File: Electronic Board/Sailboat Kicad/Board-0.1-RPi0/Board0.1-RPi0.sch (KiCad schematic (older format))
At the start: 22 parts, among them J1 Conn_02x20_Odd_Even, J10 Conn_01x03, J11 Conn_01x03, J12 Conn_01x03, J2 Conn_02x12_Odd_Even, J3 Conn_01x01, J4 Conn_02x12_Odd_Even, J5 Conn_01x01, J6 Conn_02x12_Odd_Even, J7 Conn_01x02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

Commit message: Removed the arduino. Why keep it?? Doesn't make sense :/
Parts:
- removed J2, J4, J6: Conn_02x12_Odd_Even, Pin_Headers:Pin_Header_Straight_2x12_Pitch2.54mm, symbol Conn_02x12_Odd_Even
- removed J3, J5: Conn_01x01, Pin_Headers:Pin_Header_Straight_1x01_Pitch2.54mm, symbol Conn_01x01
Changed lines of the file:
@@
 $EndComp
-$Comp
-L Conn_02x12_Odd_Even J2
-U 1 1 5B9A869B
-P 1200 6950
-F 0 "J2" H 1250 7550 50  0000 C CNN
-F 1 "Conn_02x12_Odd_Even" H 1250 6250 50  0000 C CNN
-F 2 "Pin_Headers:Pin_Header_Straight_2x12_Pitch2.54mm" H 1200 6950 50  0001 C CNN
-F 3 "" H 1200 6950 50  0001 C CNN
-	1    1200 6950
-	1    0    0    1
-$EndComp
-$Comp
-L Conn_02x12_Odd_Even J4
-U 1 1 5B9A86F0
-P 2500 5450
-F 0 "J4" H 2550 6050 50  0000 C CNN
-F 1 "Conn_02x12_Odd_Even" H 2550 4750 50  0000 C CNN
-F 2 "Pin_Headers:Pin_Header_Straight_2x12_Pitch2.54mm" H 2500 5450 50  0001 C CNN
-F 3 "" H 2500 5450 50  0001 C CNN
-	1    2500 5450
-	0    1    -1   0
-$EndComp
-$Comp
-L Conn_02x12_Odd_Even J6
-U 1 1 5B9A8755
-P 3700 6950
-F 0 "J6" H 3750 7550 50  0000 C CNN
-F 1 "Conn_02x12_Odd_Even" H 3750 6250 50  0000 C CNN
-F 2 "Pin_Headers:Pin_Header_Straight_2x12_Pitch2.54mm" H 3700 6950 50  0001 C CNN
-F 3 "" H 3700 6950 50  0001 C CNN
-	1    3700 6950
-	1    0    0    1
-$EndComp
-$Comp
-L Conn_01x01 J3
-U 1 1 5B9A8817
-P 1200 5600
-F 0 "J3" H 1200 5700 50  0000 C CNN
-F 1 "Conn_01x01" H 1200 5500 50  0000 C CNN
-F 2 "Pin_Headers:Pin_Header_Straight_1x01_Pitch2.54mm" H 1200 5600 50  0001 C CNN
-F 3 "" H 1200 5600 50  0001 C CNN
-	1    1200 5600
-	1    0    0    -1
-$EndComp
-$Comp
-L Conn_01x01 J5
-U 1 1 5B9A8879
-P 3600 5600
-F 0 "J5" H 3600 5700 50  0000 C CNN
-F 1 "Conn_01x01" H 3600 5500 50  0000 C CNN
-F 2 "Pin_Headers:Pin_Header_Straight_1x01_Pitch2.54mm" H 3600 5600 50  0001 C CNN
-F 3 "" H 3600 5600 50  0001 C CNN
-	1    3600 5600
-	-1   0    0    1
-$EndComp
-$Comp
-L GND #PWR01
-U 1 1 5B9A8D5B
-P 4100 7450
-F 0 "#PWR01" H 4100 7200 50  0001 C CNN
-F 1 "GND" H 4100 7300 50  0000 C CNN
-F 2 "" H 4100 7450 50  0001 C CNN
-F 3 "" H 4100 7450 50  0001 C CNN
-	1    4100 7450
-	1    0    0    -1
-$EndComp
-Wire Wire Line
-	4100 7450 4000 7450
-Wire Wire Line
-	3400 7450 3500 7450
 $Comp
 L +5V #PWR02
@@
 Wire Wire Line
 	2900 800  2800 800
-$Comp
-L +5V #PWR05
-U 1 1 5B9A8D99
-P 3400 7450
-F 0 "#PWR05" H 3400 7300 50  0001 C CNN
-F 1 "+5V" H 3400 7590 50  0000 C CNN
-F 2 "" H 3400 7450 50  0001 C CNN
-F 3 "" H 3400 7450 50  0001 C CNN
-	1    3400 7450
-	-1   0    0    1
-$EndComp
 Text GLabel 5150 800  0    60   Input ~ 0
 BAT+

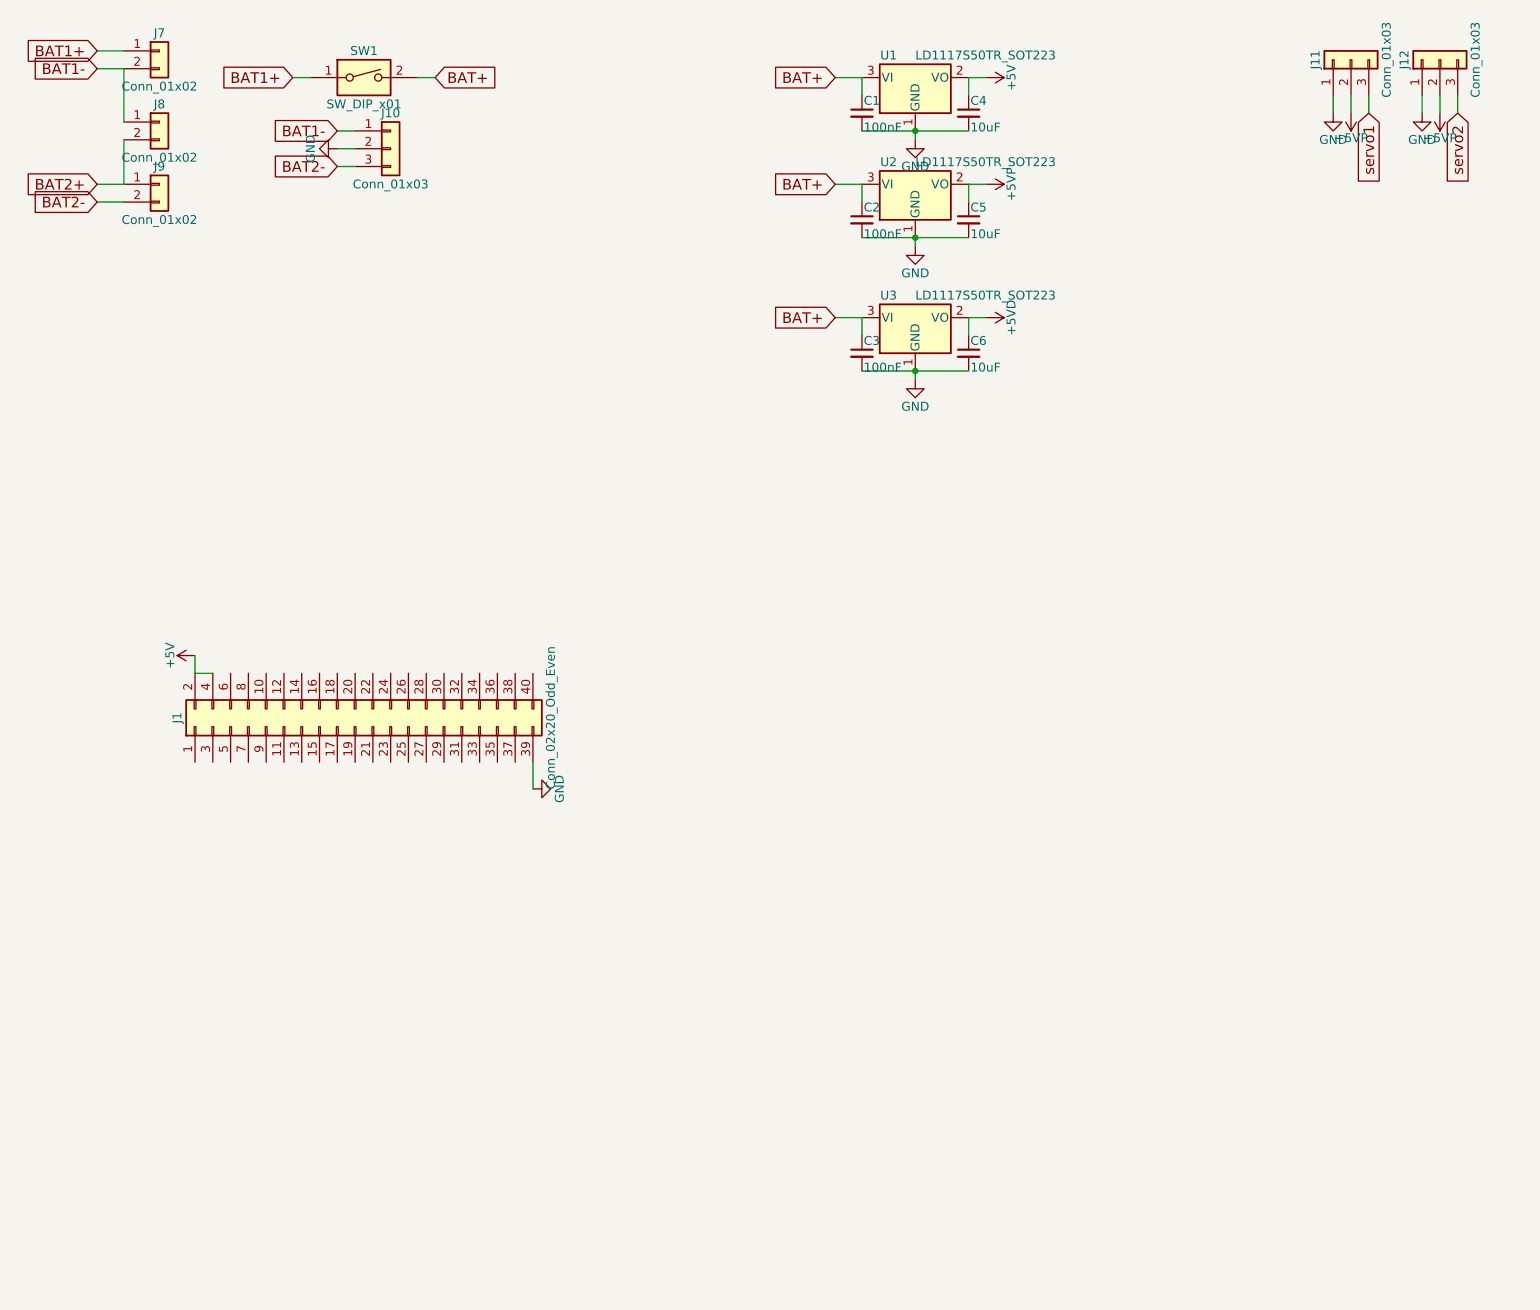
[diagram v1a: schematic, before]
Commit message: Components installed for a working rpi0 shield for sailboat
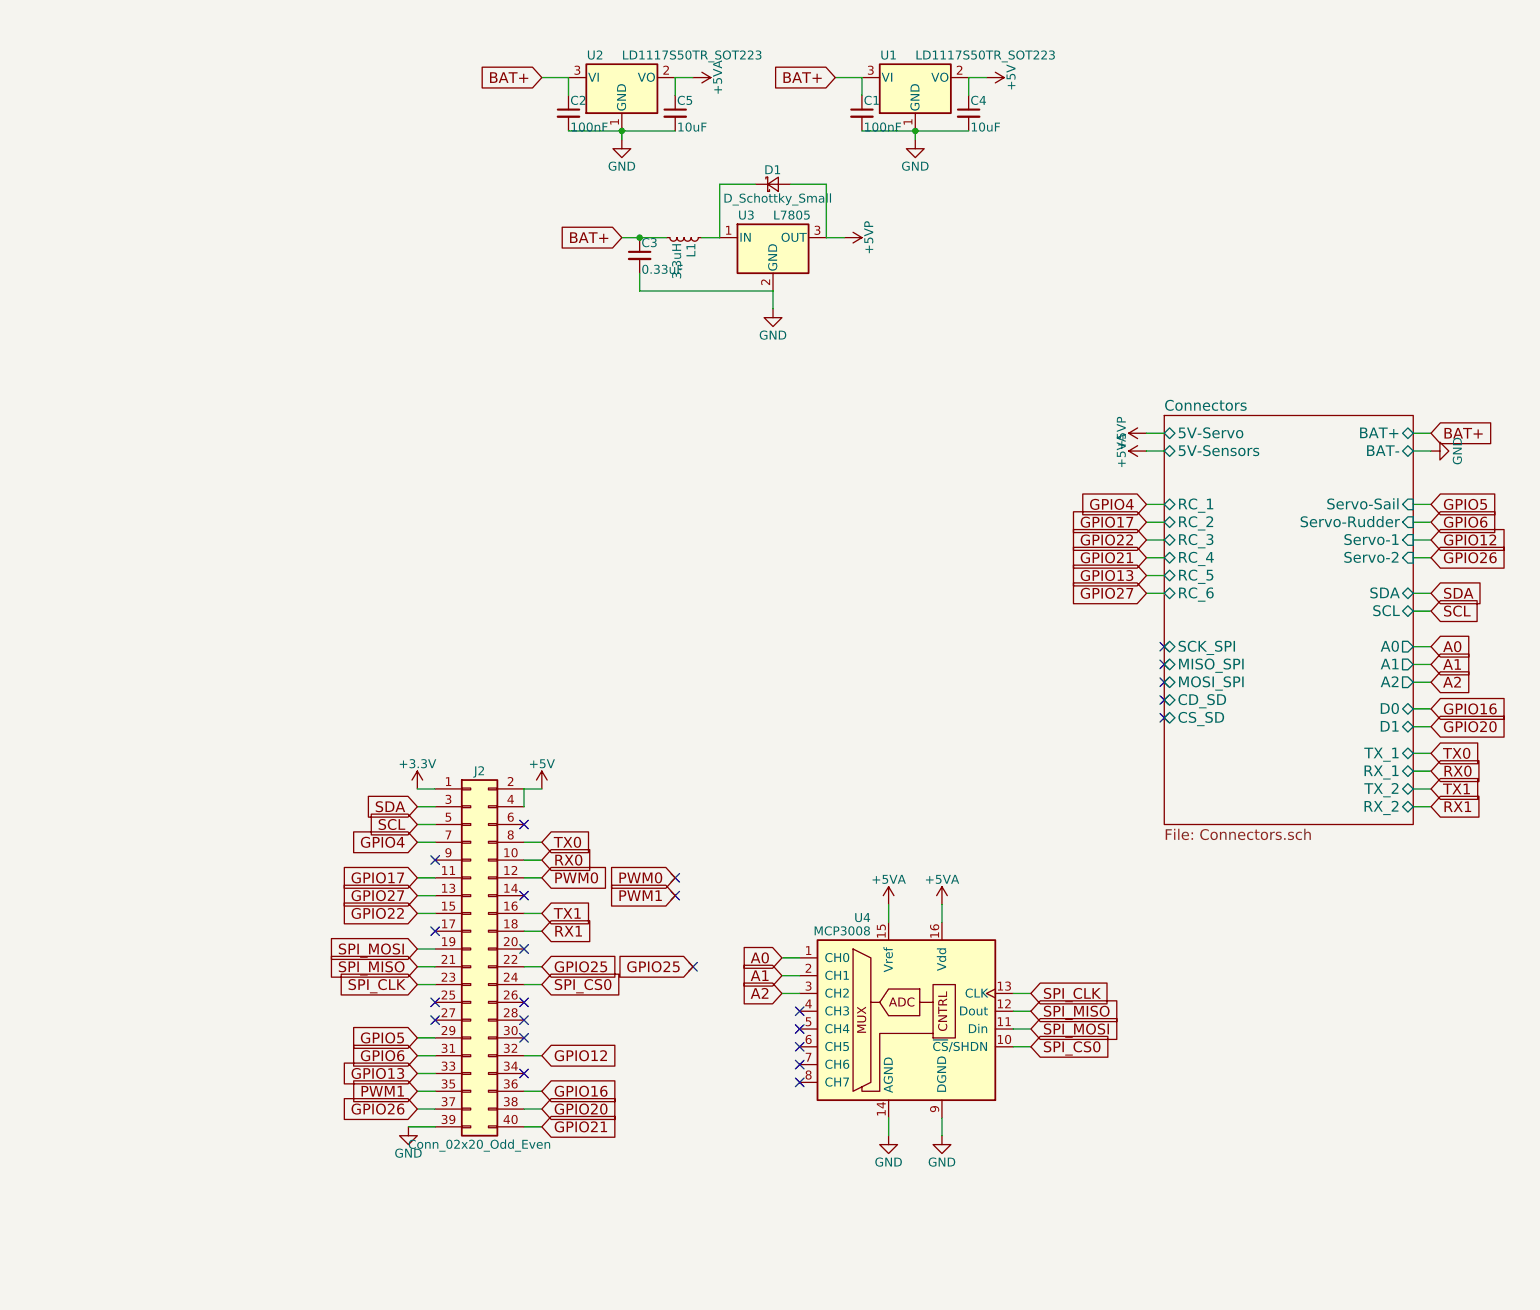
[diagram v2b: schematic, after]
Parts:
- removed C6: 10uF, Capacitors_SMD:C_0603, symbol C_Small
- removed J1: Conn_02x20_Odd_Even, Pin_Headers:Pin_Header_Straight_2x20_Pitch2.54mm, symbol Conn_02x20_Odd_Even
- removed J10: Conn_01x03, Pin_Headers:Pin_Header_Straight_1x03_Pitch2.54mm, symbol Conn_01x03
- removed J11, J12: Conn_01x03, Pin_Headers:Pin_Header_Angled_1x03_Pitch2.54mm, symbol Conn_01x03
- removed J7, J8, J9: Conn_01x02, Pin_Headers:Pin_Header_Straight_1x02_Pitch2.54mm, symbol Conn_01x02
- removed SW1: SW_DIP_x01, Buttons_Switches_THT:SW_DIP_x1_W7.62mm_Slide, symbol SW_DIP_x01
- removed U3: LD1117S50TR_SOT223, TO_SOT_Packages_SMD:SOT-223-3_TabPin2, symbol LD1117S50TR_SOT223
- added D1: D_Schottky_Small, Diodes_SMD:D_1206, symbol D_Schottky_Small
- added J2: Conn_02x20_Odd_Even, Pin_Headers:Pin_Header_Straight_2x20_Pitch2.54mm, symbol Conn_02x20_Odd_Even
- added L1: 3.3uH, Inductors_SMD:L_0603, symbol L_Small
- added U3: L7805, TO_SOT_Packages_THT:TO-220-3_Vertical, symbol L7805
- added U4: MCP3008, Housings_SOIC:SOIC-16_3.9x9.9mm_Pitch1.27mm, symbol MCP3008
- C3: value 100nF -> 0.33uF
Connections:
- net +5V: now also J2.2 (Pin_2), J2.4 (Pin_4)
- net +5VP: now also D1.2 (A), U3.3 (OUT); no longer C5.1, U2.2 (VO)
- net BAT+: now also L1.2
- net GND: now also J2.39 (Pin_39), U3.2 (GND), U4.14 (AGND), U4.9 (DGND)
- new net: D1.1 (K), L1.1, U3.1 (IN)
- new net +3V3: J2.1 (Pin_1)
- new net +5VA: C5.1, U2.2 (VO), U4.15 (Vref), U4.16 (Vdd)
- new net A0: U4.1 (CH0)
- new net A1: U4.2 (CH1)
- new net A2: U4.3 (CH2)
- new net GPIO12: J2.32 (Pin_32)
- new net GPIO13: J2.33 (Pin_33)
- new net GPIO16: J2.36 (Pin_36)
- new net GPIO17: J2.11 (Pin_11)
- new net GPIO20: J2.38 (Pin_38)
- new net GPIO21: J2.40 (Pin_40)
- new net GPIO22: J2.15 (Pin_15)
- new net GPIO25: J2.22 (Pin_22)
- new net GPIO26: J2.37 (Pin_37)
- new net GPIO27: J2.13 (Pin_13)
- new net GPIO4: J2.7 (Pin_7)
- new net GPIO5: J2.29 (Pin_29)
- new net GPIO6: J2.31 (Pin_31)
- new net PWM0: J2.12 (Pin_12)
- new net PWM1: J2.35 (Pin_35)
- new net RX0: J2.10 (Pin_10)
- new net RX1: J2.18 (Pin_18)
- new net SCL: J2.5 (Pin_5)
- new net SDA: J2.3 (Pin_3)
- new net SPI_CLK: J2.23 (Pin_23), U4.13 (CLK)
- new net SPI_CS0: J2.24 (Pin_24), U4.10 (~CS~/SHDN)
- new net SPI_MISO: J2.21 (Pin_21), U4.12 (Dout)
- new net SPI_MOSI: J2.19 (Pin_19), U4.11 (Din)
- new net TX0: J2.8 (Pin_8)
- new net TX1: J2.16 (Pin_16)
- no-connect marks 0 -> 24

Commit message: Finished tracing the RPi0 Board and plotted the gerbers, ready for production
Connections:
- net GPIO13: now also J2.18 (Pin_18); no longer J2.33 (Pin_33)
- net GPIO21: now also J2.16 (Pin_16); no longer J2.40 (Pin_40)
- net RX1: now also J2.33 (Pin_33); no longer J2.18 (Pin_18)
- net TX1: now also J2.40 (Pin_40); no longer J2.16 (Pin_16)
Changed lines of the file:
@@
 $EndDescr
 $Comp
-L +5V #PWR3
+L +5V #PWR01
 U 1 1 5B9A8F7E
 P 3500 4800
-F 0 "#PWR3" H 3500 4650 50  0001 C CNN
+F 0 "#PWR01" H 3500 4650 50  0001 C CNN
 F 1 "+5V" H 3500 4940 50  0000 C CNN
 F 2 "" H 3500 4800 50  0001 C CNN
@@
 	3400 4800 3500 4800
 $Comp
-L GND #PWR1
+L GND #PWR02
 U 1 1 5B9A9240
 P 2750 6700
-F 0 "#PWR1" H 2750 6450 50  0001 C CNN
+F 0 "#PWR02" H 2750 6450 50  0001 C CNN
 F 1 "GND" H 2750 6550 50  0000 C CNN
 F 2 "" H 2750 6700 50  0001 C CNN
@@
 	5300 800  5150 800
 $Comp
-L GND #PWR10
+L GND #PWR03
 U 1 1 5B9AA109
 P 5600 1150
-F 0 "#PWR10" H 5600 900 50  0001 C CNN
+F 0 "#PWR03" H 5600 900 50  0001 C CNN
 F 1 "GND" H 5600 1000 50  0000 C CNN
 F 2 "" H 5600 1150 50  0001 C CNN
@@
 	5300 900  5300 800
 $Comp
-L +5V #PWR13
+L +5V #PWR04
 U 1 1 5B9AA581
 P 6000 800
-F 0 "#PWR13" H 6000 650 50  0001 C CNN
+F 0 "#PWR04" H 6000 650 50  0001 C CNN
 F 1 "+5V" H 6000 940 50  0000 C CNN
 F 2 "" H 6000 800 50  0001 C CNN
@@
 $EndComp
 $Comp
-L GND #PWR6
+L GND #PWR05
 U 1 1 5B9C3518
 P 4800 2100
-F 0 "#PWR6" H 4800 1850 50  0001 C CNN
+F 0 "#PWR05" H 4800 1850 50  0001 C CNN
 F 1 "GND" H 4800 1950 50  0000 C CNN
 F 2 "" H 4800 2100 50  0001 C CNN
@@
 	4500 1400 4500 1700
 $Comp
-L +5VP #PWR7
+L +5VP #PWR06
 U 1 1 5B9C3F03
 P 5200 1700
-F 0 "#PWR7" H 5200 1550 50  0001 C CNN
+F 0 "#PWR06" H 5200 1550 50  0001 C CNN
 F 1 "+5VP" H 5200 1840 50  0000 C CNN
 F 2 "" H 5200 1700 50  0001 C CNN
@@
 	3650 800  3500 800
 $Comp
-L GND #PWR4
+L GND #PWR07
 U 1 1 5B9C4441
 P 3950 1150
-F 0 "#PWR4" H 3950 900 50  0001 C CNN
+F 0 "#PWR07" H 3950 900 50  0001 C CNN
 F 1 "GND" H 3950 1000 50  0000 C CNN
 F 2 "" H 3950 1150 50  0001 C CNN
@@
 	4250 800  4350 800
 $Comp
-L +5VA #PWR5
+L +5VA #PWR08
 U 1 1 5B9C4536
 P 4350 800
-F 0 "#PWR5" H 4350 650 50  0001 C CNN
+F 0 "#PWR08" H 4350 650 50  0001 C CNN
 F 1 "+5VA" H 4350 940 50  0000 C CNN
 F 2 "" H 4350 800 50  0001 C CNN
@@
 BAT+
 $Comp
-L GND #PWR16
+L GND #PWR09
 U 1 1 5B9C5112
 P 8500 2900
-F 0 "#PWR16" H 8500 2650 50  0001 C CNN
+F 0 "#PWR09" H 8500 2650 50  0001 C CNN
 F 1 "GND" H 8500 2750 50  0000 C CNN
 F 2 "" H 8500 2900 50  0001 C CNN
@@
 	8500 2900 8400 2900
 $Comp
-L +5VP #PWR14
+L +5VP #PWR010
 U 1 1 5B9C5BCD
 P 6900 2800
-F 0 "#PWR14" H 6900 2650 50  0001 C CNN
+F 0 "#PWR010" H 6900 2650 50  0001 C CNN
 F 1 "+5VP" H 6900 2940 50  0000 C CNN
 F 2 "" H 6900 2800 50  0001 C CNN
@@
 $EndComp
 $Comp
-L +5VA #PWR15
+L +5VA #PWR011
 U 1 1 5B9C5F4D
 P 6900 2900
-F 0 "#PWR15" H 6900 2750 50  0001 C CNN
+F 0 "#PWR011" H 6900 2750 50  0001 C CNN
 F 1 "+5VA" H 6900 3040 50  0000 C CNN
 F 2 "" H 6900 2900 50  0001 C CNN
@@
 	2900 4900 2800 4900
 $Comp
-L +3.3V #PWR2
+L +3.3V #PWR012
 U 1 1 5B9D0844
 P 2800 4800
-F 0 "#PWR2" H 2800 4650 50  0001 C CNN
+F 0 "#PWR012" H 2800 4650 50  0001 C CNN
 F 1 "+3.3V" H 2800 4940 50  0000 C CNN
 F 2 "" H 2800 4800 50  0001 C CNN
@@
 Wire Wire Line
 	2900 4800 2800 4800
-Text GLabel 3500 5500 2    60   Input ~ 0
+Text GLabel 3500 6700 2    60   Input ~ 0
 TX1
-Text GLabel 3500 5600 2    60   Input ~ 0
+Text GLabel 2800 6400 0    60   Input ~ 0
 RX1
 Wire Wire Line
@@
 NoConn ~ 4950 6450
 $Comp
-L GND #PWR12
+L GND #PWR013
 U 1 1 5B9D4F32
 P 5750 6750
-F 0 "#PWR12" H 5750 6500 50  0001 C CNN
+F 0 "#PWR013" H 5750 6500 50  0001 C CNN
 F 1 "GND" H 5750 6600 50  0000 C CNN
 F 2 "" H 5750 6750 50  0001 C CNN
@@
 $EndComp
 $Comp
-L GND #PWR9
+L GND #PWR014
 U 1 1 5B9D5477
 P 5450 6750
-F 0 "#PWR9" H 5450 6500 50  0001 C CNN
+F 0 "#PWR014" H 5450 6500 50  0001 C CNN
 F 1 "GND" H 5450 6600 50  0000 C CNN
 F 2 "" H 5450 6750 50  0001 C CNN
@@
 $EndComp
 $Comp
-L +5VA #PWR11
+L +5VA #PWR015
 U 1 1 5B9D653D
 P 5750 5450
-F 0 "#PWR11" H 5750 5300 50  0001 C CNN
+F 0 "#PWR015" H 5750 5300 50  0001 C CNN
 F 1 "+5VA" H 5750 5590 50  0000 C CNN
 F 2 "" H 5750 5450 50  0001 C CNN
@@
 $EndComp
 $Comp
-L +5VA #PWR8
+L +5VA #PWR016
 U 1 1 5B9D6C80
 P 5450 5450
-F 0 "#PWR8" H 5450 5300 50  0001 C CNN
+F 0 "#PWR016" H 5450 5300 50  0001 C CNN
 F 1 "+5VA" H 5450 5590 50  0000 C CNN
 F 2 "" H 5450 5450 50  0001 C CNN
@@
 NoConn ~ 2900 6100
 NoConn ~ 3400 6400
-Text GLabel 3500 6700 2    60   Input ~ 0
+Text GLabel 3500 5500 2    60   Input ~ 0
 GPIO21
 Wire Wire Line
@@
 Text GLabel 6900 3500 0    60   Input ~ 0
 GPIO21
-Text GLabel 2800 6400 0    60   Input ~ 0
+Text GLabel 3500 5600 2    60   Input ~ 0
 GPIO13
 Wire Wire Line
